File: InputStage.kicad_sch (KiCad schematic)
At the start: 4 parts, among them SW1 218-8LPSTR, SW44 SW_DIP_x02

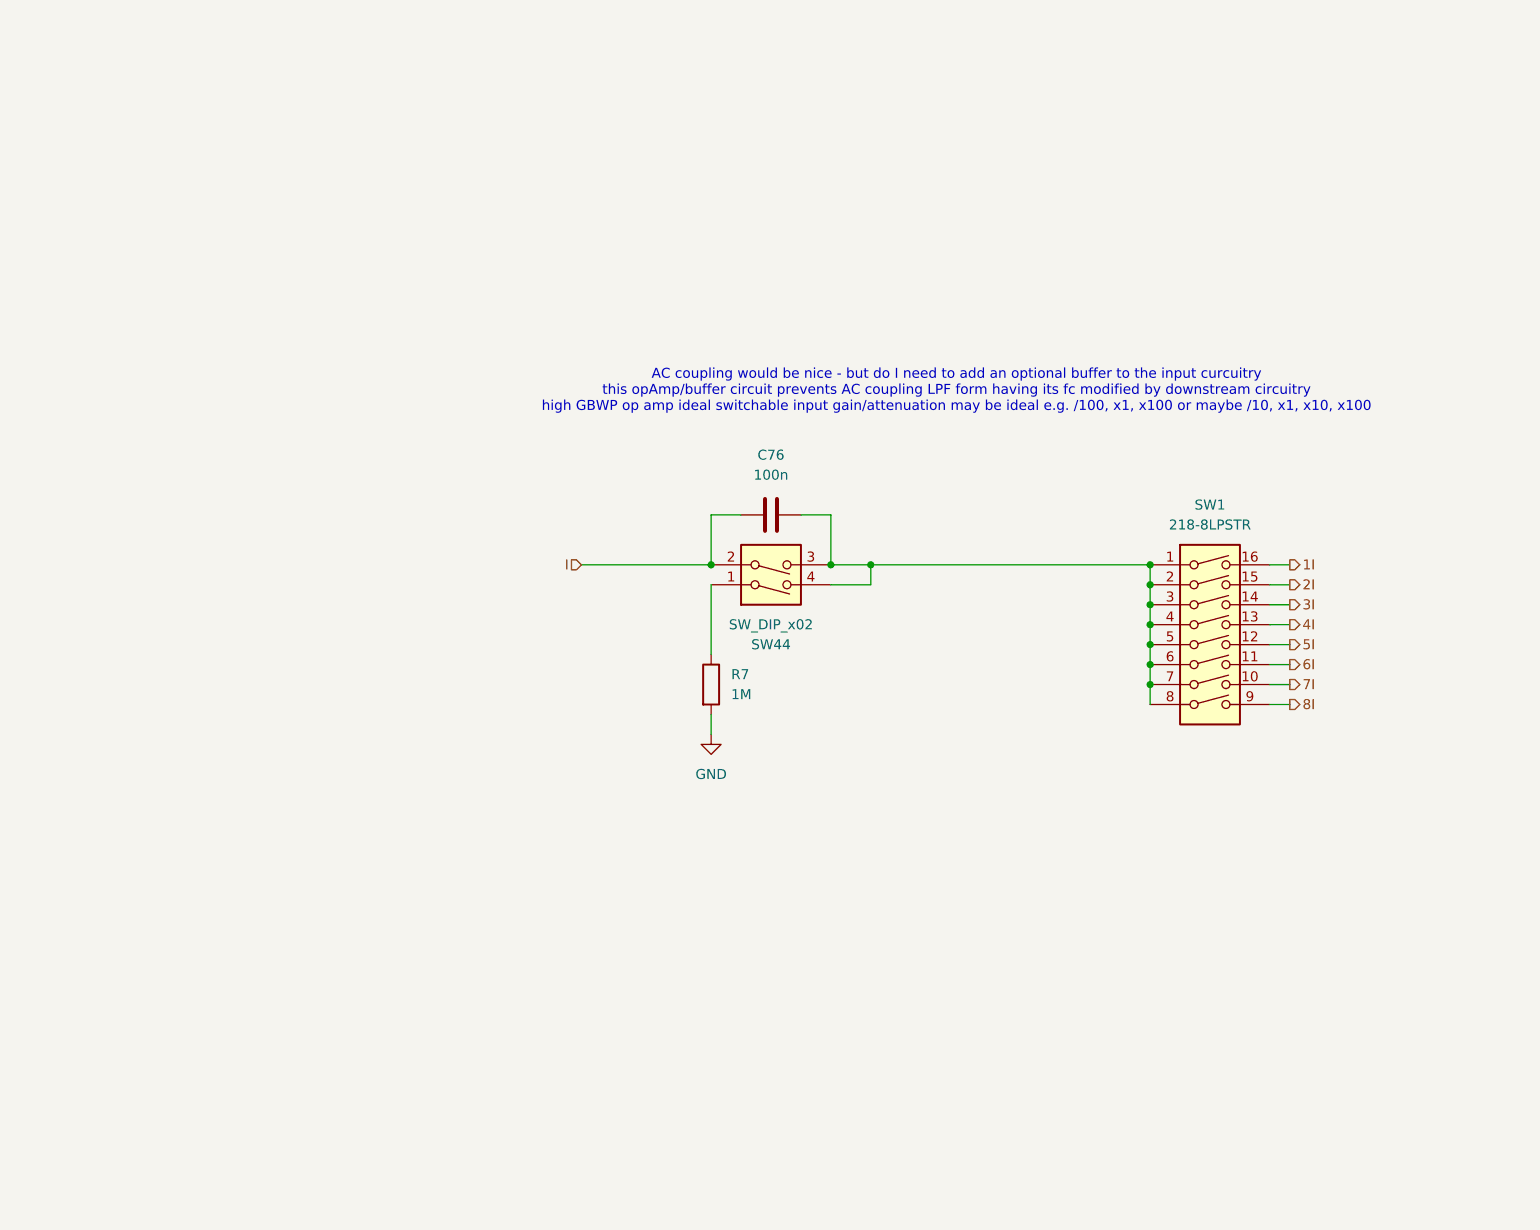
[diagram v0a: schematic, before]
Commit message: preliminary layout of op amp blocks complete
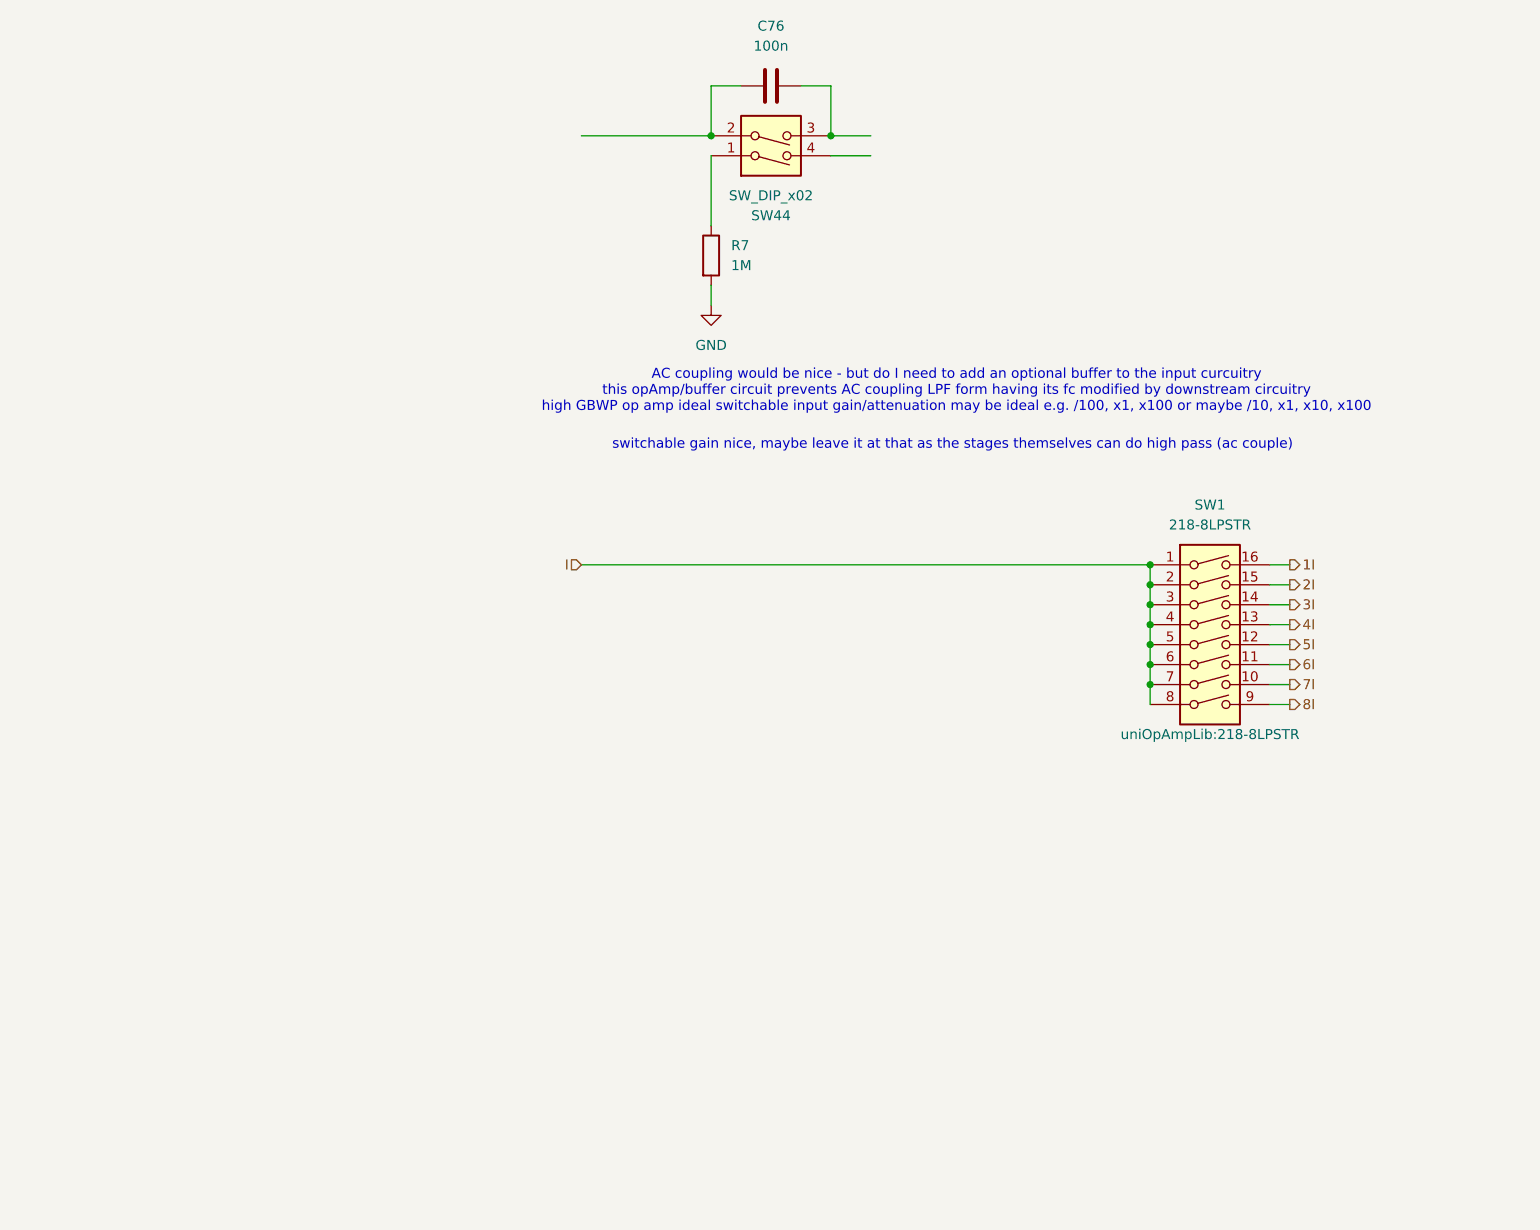
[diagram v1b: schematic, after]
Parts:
- SW1: footprint (none) -> uniOpAmpLib:218-8LPSTR
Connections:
- net I: now also SW1.1, SW1.2, SW1.3, SW1.4, SW1.5, SW1.6, SW1.7, SW1.8; no longer C76.1, SW44.2
- new net: C76.1, SW44.2
- new net: C76.2, SW44.3
- now unconnected: SW44.4
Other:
- note added: "switchable gain nice, maybe leave it at that as the stages themselves can do high pass (ac couple)"
- moved on the sheet: C76, R7, SW44
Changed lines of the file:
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@@
+		)
+	)
+	(text "switchable gain nice, maybe leave it at that as the stages themselves can do high pass (ac couple)"
+		(exclude_from_sim no)
+		(at 148.844 69.85 0)
+		(effects
+			(font
+				(size 1.27 1.27)
+			)
 		)
 	)
@@
 	)
 	(junction
-		(at 138.43 85.09)
-		(diameter 0)
-		(color 0 0 0 0)
-	)
-	(junction
 		(at 173.99 95.25)
 		(diameter 0)
@@
 	)
 	(junction
-		(at 133.35 85.09)
+		(at 133.35 30.48)
 		(diameter 0)
 		(color 0 0 0 0)
 	)
 	(junction
-		(at 118.11 85.09)
+		(at 118.11 30.48)
 		(diameter 0)
 		(color 0 0 0 0)
@@
 	(wire
 		(pts
-			(xy 138.43 87.63) (xy 138.43 85.09)
-		)
-		(stroke
-			(width 0)
-			(type default)
-		)
-	)
-	(wire
-		(pts
-			(xy 133.35 78.74) (xy 133.35 85.09)
+			(xy 133.35 24.13) (xy 133.35 30.48)
 		)
 		(stroke
@@
 	(wire
 		(pts
-			(xy 133.35 85.09) (xy 138.43 85.09)
+			(xy 133.35 30.48) (xy 138.43 30.48)
 		)
 		(stroke
@@
 	(wire
 		(pts
-			(xy 118.11 87.63) (xy 118.11 96.52)
+			(xy 118.11 33.02) (xy 118.11 41.91)
 		)
 		(stroke
@@
 	(wire
 		(pts
-			(xy 118.11 85.09) (xy 118.11 78.74)
+			(xy 118.11 30.48) (xy 118.11 24.13)
 		)
 		(stroke
@@
 	(wire
 		(pts
-			(xy 133.35 87.63) (xy 138.43 87.63)
+			(xy 133.35 33.02) (xy 138.43 33.02)
+		)
+		(stroke
+			(width 0)
+			(type default)
+		)
+	)
+	(wire
+		(pts
+			(xy 101.6 85.09) (xy 173.99 85.09)
 		)
 		(stroke
@@
 	(wire
 		(pts
-			(xy 138.43 85.09) (xy 173.99 85.09)
-		)
-		(stroke
-			(width 0)
-			(type default)
-		)
-	)
-	(wire
-		(pts
-			(xy 118.11 78.74) (xy 121.92 78.74)
-		)
-		(stroke
-			(width 0)
-			(type default)
-		)
-	)
-	(wire
-		(pts
-			(xy 129.54 78.74) (xy 133.35 78.74)
+			(xy 118.11 24.13) (xy 121.92 24.13)
+		)
+		(stroke
+			(width 0)
+			(type default)
+		)
+	)
+	(wire
+		(pts
+			(xy 129.54 24.13) (xy 133.35 24.13)
 		)
 		(stroke
@@
 	(wire
 		(pts
-			(xy 118.11 106.68) (xy 118.11 104.14)
+			(xy 118.11 52.07) (xy 118.11 49.53)
 		)
 		(stroke
@@
 	(wire
 		(pts
-			(xy 101.6 85.09) (xy 118.11 85.09)
+			(xy 101.6 30.48) (xy 118.11 30.48)
 		)
 		(stroke
@@
 	(symbol
 		(lib_id "power:GND")
-		(at 118.11 106.68 0)
+		(at 118.11 52.07 0)
 		(unit 1)
 		(body_style 1)
@@
 		(fields_autoplaced yes)
 		(property "Reference" "#PWR057"
-			(at 118.11 113.03 0)
+			(at 118.11 58.42 0)
 			(hide yes)
 			(show_name no)
@@
 		)
 		(property "Value" "GND"
-			(at 118.11 111.76 0)
+			(at 118.11 57.15 0)
 			(show_name no)
 			(do_not_autoplace no)
@@
 		)
 		(property "Footprint" ""
-			(at 118.11 106.68 0)
+			(at 118.11 52.07 0)
 			(hide yes)
 			(show_name no)
@@
 		)
 		(property "Datasheet" ""
-			(at 118.11 106.68 0)
+			(at 118.11 52.07 0)
 			(hide yes)
 			(show_name no)
@@
 		)
 		(property "Description" "Power symbol creates a global label with name \"GND\" , ground"
-			(at 118.11 106.68 0)
+			(at 118.11 52.07 0)
 			(hide yes)
 			(show_name no)
@@
 		(instances
 			(project "universalOpAmpV0"
+				(path "/0c9d5097-e341-4aa8-a29f-4bc5e653f52f/248e0a52-6ac7-4573-b180-c7bb6a408c88"
+					(reference "#PWR067")
+					(unit 1)
+				)
 				(path "/0c9d5097-e341-4aa8-a29f-4bc5e653f52f/48d355b3-237b-4228-9d01-e6a4bd4e5c45"
 					(reference "#PWR057")
 					(unit 1)
 				)
+				(path "/0c9d5097-e341-4aa8-a29f-4bc5e653f52f/a2242a1b-24c1-41af-bbc9-90925611ea53"
+					(reference "#PWR068")
+					(unit 1)
+				)
 			)
 		)
@@
 	(symbol
 		(lib_id "Device:C")
-		(at 125.73 78.74 90)
+		(at 125.73 24.13 90)
 		(unit 1)
 		(body_style 1)
@@
 		(fields_autoplaced yes)
 		(property "Reference" "C76"
-			(at 125.73 71.12 90)
+			(at 125.73 16.51 90)
 			(show_name no)
 			(do_not_autoplace no)
@@
 		)
 		(property "Value" "100n"
-			(at 125.73 73.66 90)
+			(at 125.73 19.05 90)
 			(show_name no)
 			(do_not_autoplace no)
@@
 		)
 		(property "Footprint" ""
-			(at 129.54 77.7748 0)
+			(at 129.54 23.1648 0)
 			(hide yes)
 			(show_name no)
@@
 		)
 		(property "Datasheet" ""
-			(at 125.73 78.74 0)
+			(at 125.73 24.13 0)
 			(hide yes)
 			(show_name no)
@@
 		)
 		(property "Description" "Unpolarized capacitor"
-			(at 125.73 78.74 0)
+			(at 125.73 24.13 0)
 			(hide yes)
 			(show_name no)
@@
 		(instances
 			(project "universalOpAmpV0"
+				(path "/0c9d5097-e341-4aa8-a29f-4bc5e653f52f/248e0a52-6ac7-4573-b180-c7bb6a408c88"
+					(reference "C78")
+					(unit 1)
+				)
 				(path "/0c9d5097-e341-4aa8-a29f-4bc5e653f52f/48d355b3-237b-4228-9d01-e6a4bd4e5c45"
 					(reference "C76")
+					(unit 1)
+				)
+				(path "/0c9d5097-e341-4aa8-a29f-4bc5e653f52f/a2242a1b-24c1-41af-bbc9-90925611ea53"
+					(reference "C79")
 					(unit 1)
 				)
@@
 		(in_pos_files yes)
 		(dnp no)
-		(fields_autoplaced yes)
 		(property "Reference" "SW1"
 			(at 181.61 77.47 0)
@@
 			)
 		)
-		(property "Footprint" ""
-			(at 181.61 95.25 0)
-			(hide yes)
+		(property "Footprint" "uniOpAmpLib:218-8LPSTR"
+			(at 181.61 106.68 0)
 			(show_name no)
 			(do_not_autoplace no)
@@
 		(instances
 			(project "universalOpAmpV0"
+				(path "/0c9d5097-e341-4aa8-a29f-4bc5e653f52f/248e0a52-6ac7-4573-b180-c7bb6a408c88"
+					(reference "SW47")
+					(unit 1)
+				)
 				(path "/0c9d5097-e341-4aa8-a29f-4bc5e653f52f/48d355b3-237b-4228-9d01-e6a4bd4e5c45"
 					(reference "SW1")
 					(unit 1)
 				)
+				(path "/0c9d5097-e341-4aa8-a29f-4bc5e653f52f/a2242a1b-24c1-41af-bbc9-90925611ea53"
+					(reference "SW49")
+					(unit 1)
+				)
 			)
 		)
@@
 	(symbol
 		(lib_id "Device:R")
-		(at 118.11 100.33 0)
+		(at 118.11 45.72 0)
 		(unit 1)
 		(body_style 1)
@@
 		(fields_autoplaced yes)
 		(property "Reference" "R7"
-			(at 120.65 99.0599 0)
+			(at 120.65 44.4499 0)
 			(show_name no)
 			(do_not_autoplace no)
@@
 		)
 		(property "Value" "1M"
-			(at 120.65 101.5999 0)
+			(at 120.65 46.9899 0)
 			(show_name no)
 			(do_not_autoplace no)
@@
 		)
 		(property "Footprint" ""
-			(at 116.332 100.33 90)
+			(at 116.332 45.72 90)
 			(hide yes)
 			(show_name no)
@@
 		)
 		(property "Datasheet" ""
-			(at 118.11 100.33 0)
+			(at 118.11 45.72 0)
 			(hide yes)
 			(show_name no)
@@
 		)
 		(property "Description" "Resistor"
-			(at 118.11 100.33 0)
+			(at 118.11 45.72 0)
 			(hide yes)
 			(show_name no)
@@
 		(instances
 			(project "universalOpAmpV0"
+				(path "/0c9d5097-e341-4aa8-a29f-4bc5e653f52f/248e0a52-6ac7-4573-b180-c7bb6a408c88"
+					(reference "R10")
+					(unit 1)
+				)
 				(path "/0c9d5097-e341-4aa8-a29f-4bc5e653f52f/48d355b3-237b-4228-9d01-e6a4bd4e5c45"
 					(reference "R7")
 					(unit 1)
 				)
+				(path "/0c9d5097-e341-4aa8-a29f-4bc5e653f52f/a2242a1b-24c1-41af-bbc9-90925611ea53"
+					(reference "R11")
+					(unit 1)
+				)
 			)
 		)
@@
 	(symbol
 		(lib_id "Switch:SW_DIP_x02")
-		(at 125.73 85.09 0)
+		(at 125.73 30.48 0)
 		(mirror x)
 		(unit 1)
@@
 		(dnp no)
 		(property "Reference" "SW44"
-			(at 125.73 95.25 0)
+			(at 125.73 40.64 0)
 			(show_name no)
 			(do_not_autoplace no)
@@
 		)
 		(property "Value" "SW_DIP_x02"
-			(at 125.73 92.71 0)
+			(at 125.73 38.1 0)
 			(show_name no)
 			(do_not_autoplace no)
@@
 		)
 		(property "Footprint" ""
-			(at 125.73 85.09 0)
+			(at 125.73 30.48 0)
 			(hide yes)
 			(show_name no)
@@
 		)
 		(property "Datasheet" ""
-			(at 125.73 85.09 0)
+			(at 125.73 30.48 0)
 			(hide yes)
 			(show_name no)
@@
 		)
 		(property "Description" "2x DIP Switch, Single Pole Single Throw (SPST) switch, small symbol"
-			(at 125.73 85.09 0)
+			(at 125.73 30.48 0)
 			(hide yes)
 			(show_name no)
@@
 		(instances
 			(project "universalOpAmpV0"
+				(path "/0c9d5097-e341-4aa8-a29f-4bc5e653f52f/248e0a52-6ac7-4573-b180-c7bb6a408c88"
+					(reference "SW46")
+					(unit 1)
+				)
 				(path "/0c9d5097-e341-4aa8-a29f-4bc5e653f52f/48d355b3-237b-4228-9d01-e6a4bd4e5c45"
 					(reference "SW44")
 					(unit 1)
 				)
+				(path "/0c9d5097-e341-4aa8-a29f-4bc5e653f52f/a2242a1b-24c1-41af-bbc9-90925611ea53"
+					(reference "SW48")
+					(unit 1)
+				)

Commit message: input stage schematic done, layout WIP
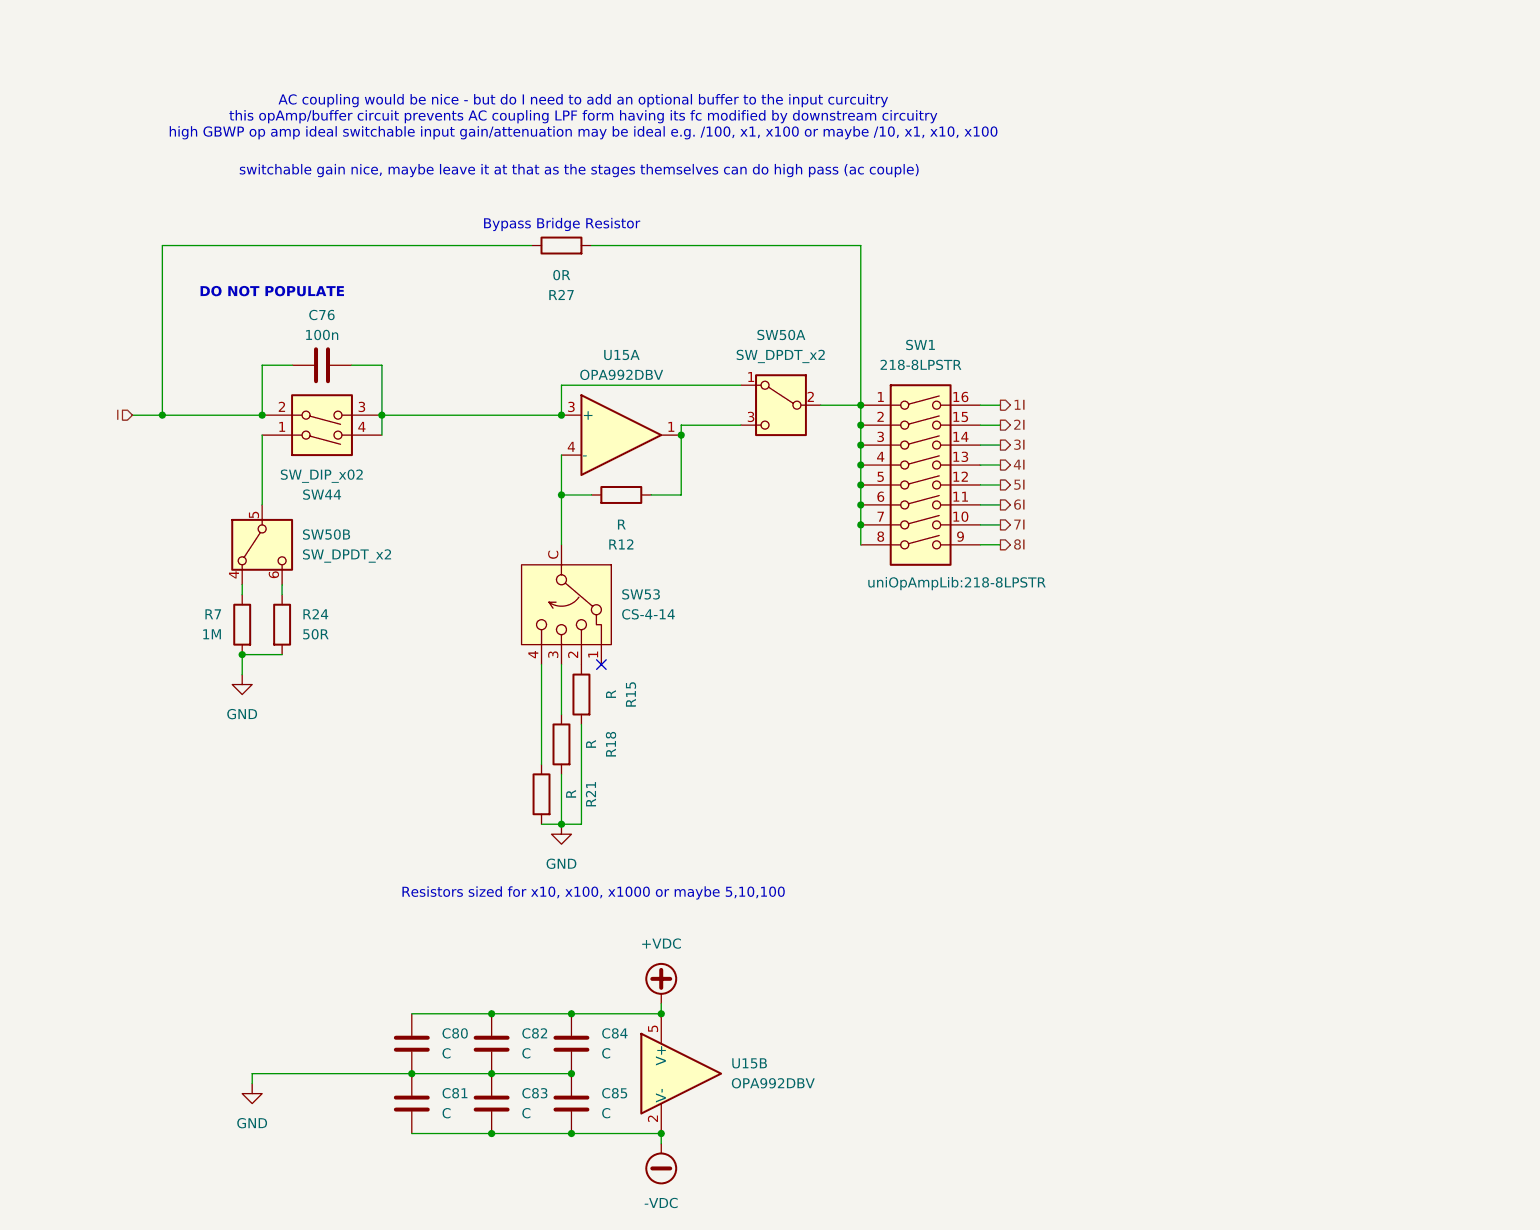
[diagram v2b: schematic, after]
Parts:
- added C80, C81, C82, C83, C84, C85: C, uniOpAmpLib:C_0805_Metric2012_HandSolder, symbol Device:C
- added R12, R15, R18, R21: R, Resistor_SMD:R_0805_2012Metric_Pad1.20x1.40mm_HandSolder, symbol Device:R
- added R24: 50R, Resistor_SMD:R_2512_6332Metric_Pad1.40x3.35mm_HandSolder, symbol Device:R
- added R27: 0R, Resistor_SMD:R_0805_2012Metric_Pad1.20x1.40mm_HandSolder, symbol Device:R
- added SW50: SW_DPDT_x2, uniOpAmpLib:CAS-DxxB, symbol Switch:SW_DPDT_x2
- added SW53: CS-4-14, uniOpAmpLib:CS-4-14NB, symbol uniOpAmpLib:CS-4-14
- added U15: OPA992DBV, uniOpAmpLib:SOT-23-5_HandSoldering, symbol uniOpAmpLib:OPA992DBV
- C76: footprint (none) -> uniOpAmpLib:PP_CAP
- R7: footprint (none) -> Resistor_SMD:R_0805_2012Metric_Pad1.20x1.40mm_HandSolder
- SW44: footprint (none) -> uniOpAmpLib:218-2LPSTR
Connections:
- net GND: now also C80.2, C81.1, C82.2, C83.1, C84.2, C85.1, R15.2, R18.2, R21.2, R24.2
- net I: now also C76.1, SW44.2, R27.1; no longer SW1.1, SW1.2, SW1.3, SW1.4, SW1.5, SW1.6, SW1.7, SW1.8
- net at C76.2, SW44.3: now also SW44.4, SW50.1 (A), U15.3 (+)
- net at R7.1: now also SW50.4 (A); no longer SW44.1
- new net: R27.2, SW1.1, SW1.2, SW1.3, SW1.4, SW1.5, SW1.6, SW1.7, SW1.8, SW50.2 (B)
- new net: R12.1, SW50.3 (C), U15.1
- new net: R15.1, SW53.2
- new net: R12.2, SW53.C, U15.4 (-)
- new net: R24.1, SW50.6 (C)
- new net: SW44.1, SW50.5 (B)
- new net: R18.1, SW53.3
- new net: R21.1, SW53.4
- new net +VDC: C80.1, C82.1, C84.1, U15.5 (V+)
- new net -VDC: C81.2, C83.2, C85.2, U15.2 (V-)
- no-connect marks 0 -> 1
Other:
- note added: "Bypass Bridge Resistor"
- note added: "DO NOT POPULATE"
- note added: "Resistors sized for x10, x100, x1000 or maybe 5,10,100"
- moved on the sheet: C76, R7, SW1, SW44
